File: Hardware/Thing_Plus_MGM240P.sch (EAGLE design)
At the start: 97 parts, among them J1 THING_PLUS_LOGICAL, J2 USB Female Type C Connector, J3 QWIIC_RIGHT_ANGLE, J5 MICRO-SDFRICTION, Q1 20V/4.2A/52mΩ/1.4W, U1 MGM240P, U2 XC6222B331MR-G, U3 EFM32GG12B410F1024GL120, U4 MCP73831, U5 MAX17048, U6 M24C02-FMC6TG, U7 MX25R8035FZUIL0, Y1 CRYSTAL-48MHZ

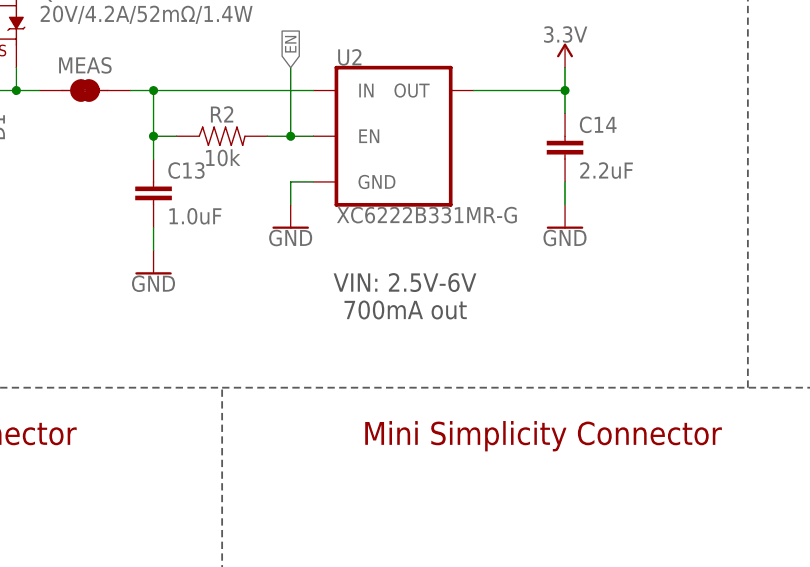
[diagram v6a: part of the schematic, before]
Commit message: Design review updates
Change voltage regulator to specify maximum input voltage only
Add Segger logo
Move traces away from jumpers to prevent accidental cutting
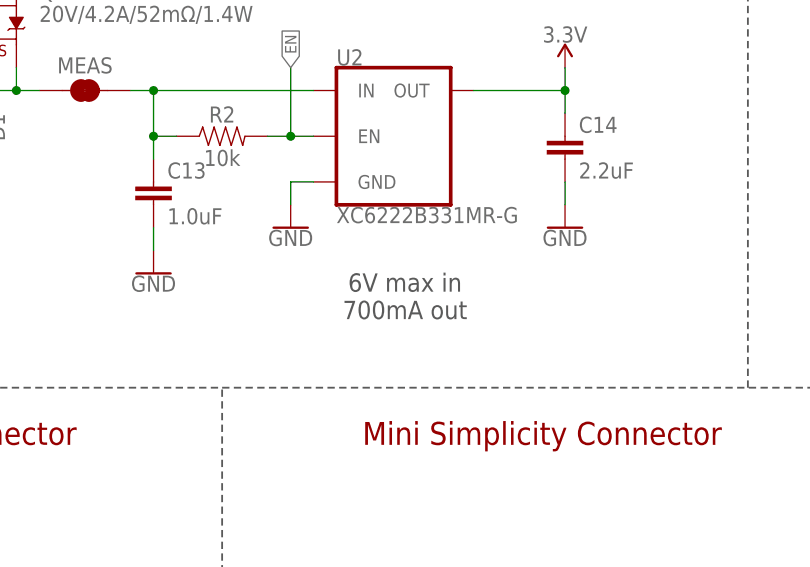
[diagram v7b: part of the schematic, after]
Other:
- note added: "6V max in 700mA out"
- note removed: "VIN: 2.5V-6V 700mA out"
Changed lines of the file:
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@@
 <text x="297.18" y="223.52" size="2.032" layer="97" font="vector" align="center">Cut and resolder jumper
 to change charge current</text>
-<text x="175.26" y="226.06" size="2.032" layer="97" font="vector" align="center">VIN: 2.5V-6V
+<text x="175.26" y="226.06" size="2.032" layer="97" font="vector" align="center">6V max in
 700mA out</text>
 <text x="17.78" y="228.6" size="2.032" layer="97" font="vector" align="center">Cut trace to isolate

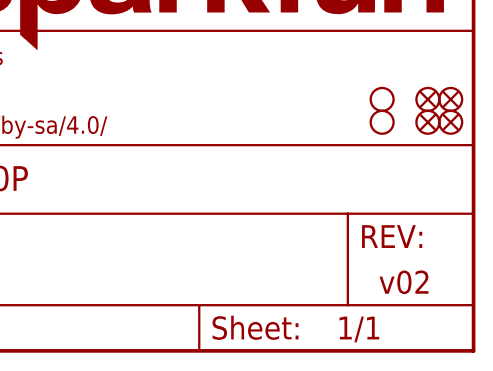
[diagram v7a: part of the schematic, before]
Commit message: Update revision number to v10
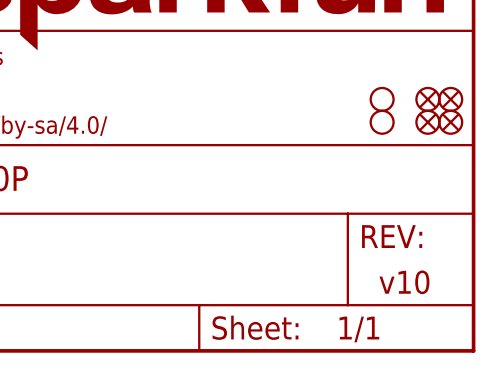
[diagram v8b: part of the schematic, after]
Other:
- note added: "v10"
- note removed: "v02"
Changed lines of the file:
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@@
 <wire x1="99.06" y1="149.86" x2="0" y2="149.86" width="0.2032" layer="97" style="longdash"/>
 <text x="358.14" y="12.7" size="2.54" layer="94" font="vector" align="center">Dryw Wade</text>
-<text x="424.18" y="7.62" size="2.54" layer="94" font="vector" align="center">v02</text>
+<text x="424.18" y="7.62" size="2.54" layer="94" font="vector" align="center">v10</text>
 <text x="20.32" y="205.74" size="2.032" layer="97" font="vector" rot="R180" align="center">Cut trace to
 remove power LED</text>
